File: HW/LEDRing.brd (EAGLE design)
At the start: 52.5 x 52.4 mm, 36 parts, among them U1 ATMEGA328P-AU, U2 MCP73831, U3 MIC5219 3.3V, U4 MMA8452Q, Y1 16MHZ

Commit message: Removed some files.
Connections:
- removed net VCCIO: U$1.4
- new net N$31: U$1.17, U$1.4
- net RESET: now also U$1.2
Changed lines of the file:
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@@
 <layer number="24" name="bOrigins" color="15" fill="1" visible="yes" active="yes"/>
 <layer number="25" name="tNames" color="7" fill="1" visible="yes" active="yes"/>
-<layer number="26" name="bNames" color="7" fill="1" visible="yes" active="yes"/>
+<layer number="26" name="bNames" color="7" fill="1" visible="no" active="yes"/>
 <layer number="27" name="tValues" color="7" fill="1" visible="yes" active="yes"/>
-<layer number="28" name="bValues" color="7" fill="1" visible="yes" active="yes"/>
+<layer number="28" name="bValues" color="7" fill="1" visible="no" active="yes"/>
 <layer number="29" name="tStop" color="7" fill="3" visible="no" active="yes"/>
 <layer number="30" name="bStop" color="7" fill="6" visible="no" active="yes"/>
@@
 <wire x1="23.241" y1="44.323" x2="21.717" y2="42.799" width="0.3048" layer="1"/>
 <wire x1="21.717" y1="42.799" x2="21.717" y2="30.988" width="0.3048" layer="1"/>
+<contactref element="U$1" pad="2"/>
+<wire x1="19.285" y1="23.341" x2="17.399" y2="30.988" width="0" layer="19" extent="1-16"/>
 </signal>
 <signal name="N$9">
@@
 <wire x1="16.51" y1="38.735" x2="16.51" y2="34.671" width="0.3048" layer="1"/>
 </signal>
-<signal name="VCCIO">
+<signal name="N$6">
+</signal>
+<signal name="N$31">
 <contactref element="U$1" pad="4"/>
-</signal>
-<signal name="N$6">
+<contactref element="U$1" pad="17"/>
+<wire x1="25.785" y1="16.029" x2="20.585" y2="23.341" width="0" layer="19" extent="16-16"/>
 </signal>
 </signals>

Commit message: Adding PCB changes for next version.
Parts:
- added C8: (no value), SparkFun-Capacitors:0603-CAP
- added D13: (no value), SparkFun-LED:LED-0603
- added JP1, JP2: JUMPER-3SMD, SparkFun-Retired:SJ_3
- added JP3: JUMPER-3-OLDSMD, SparkFun-Retired:SJ_3
- added LOGO1: OSHW-LOGOMINI, SparkFun-Aesthetics:OSHW-LOGO-MINI
- added R9: (no value), SparkFun-Passives:0603-RES
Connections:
- new net N$32: C8.1, U$1.2
- new net N$33: R9.2, U1.13
- new net N$34: D13.A, R9.1
- net GND: now also D13.C
- net RESET: now also C8.2; no longer U$1.2
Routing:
- net N$33: track 0.00 -> 22.9 mm, vias 0 -> 1
- net N$31: track 0.00 -> 11.1 mm, vias 0 -> 2
- net GND: track 202.6 -> 208.3 mm, vias 11 -> 12
- net N$32: track 0.00 -> 5.69 mm
- net 5V: track 63.7 -> 68.4 mm
- net N$4: track 14.1 -> 10.6 mm
- net RESET: track 33.6 -> 36.8 mm
- net N$15: track 33.3 -> 35.5 mm
- net V3_3: track 86.5 -> 88.4 mm
- net RX: track 10.9 -> 12.6 mm
- net N$34: track 0.00 -> 1.70 mm
- net VBATT: track 203.1 -> 204.8 mm
- net LED_DATA: track 59.5 -> 58.9 mm
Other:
- outline, holes or cut-outs redrawn

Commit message: Updated to version 1.1.
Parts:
- removed JP3: JUMPER-3-OLDSMD, SparkFun-Retired:SJ_3
- removed U$1: FT232R, GeekAmmo:SSOP-28
- added JP4: JUMPER-3SMD, SparkFun-Retired:SJ_3
- added R10: 0, SparkFun-Passives:0603-RES
- added U5: FT231XS, SparkFun-DigitalIC:SSOP20_L
- moved LOGO1 9.21 mm to (26.3, 13.8)
- moved C2 7.53 mm to (26.9, 16.8), turned to 225 degrees
- moved C4 7.49 mm to (23.4, 17.1), turned to 45 degrees
- moved J3 0.91 mm to (8.75, 24.7)
- moved D7 0.26 mm to (37.0, 44.6)
- moved D11 0.26 mm to (37.0, 7.21)
- moved D5 0.26 mm to (15.4, 44.6)
- moved D1 0.26 mm to (15.4, 7.21)
- moved D2 0.26 mm to (7.47, 15.1)
- moved D4 0.26 mm to (7.47, 36.7)
- moved D8 0.26 mm to (44.9, 36.7)
- moved D6 0.25 mm to (26.2, 47.5)
- moved D3 0.25 mm to (4.57, 25.9)
- moved D12 0.25 mm to (26.2, 4.32)
- moved D9 0.25 mm to (47.8, 25.9)
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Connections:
- removed net N$31: U$1.17, U$1.4
- removed net N$32: C8.1, U$1.2
- new net DTR: JP4.3, U5.1
- new net D_N_IN: JP1.1, JP2.1, U5.12
- new net D_N_OUT: JP1.2, U$2.P$2
- new net D_P_IN: JP1.3, JP2.3, U5.11
- new net D_P_OUT: JP2.2, U$2.P$3
- new net RTS: JP4.1, U5.2
- new net RTS_OR_DTR: C8.1, JP4.2
- net 5V: now also R10.2, U5.15; no longer U$1.20, U$2.P$1
- net GND: now also U5.16, U5.6; no longer U$1.18, U$1.21, U$1.25, U$1.26, U$1.7
- net N$4: now also R10.1, U$2.P$1; no longer U$1.16, U$2.P$2
- net N$5: now also U5.13, U5.14, U5.3; no longer U$1.15, U$2.P$3
- net RX: now also U5.20; no longer U$1.1
- net TX: now also U5.4; no longer U$1.5
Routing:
- net RTS_OR_DTR: track 0.00 -> 34.4 mm, vias 0 -> 2
- net D_P_IN: track 0.00 -> 25.7 mm, vias 0 -> 4
- net TX: track 9.58 -> 31.5 mm, vias 1 -> 4
- net D_N_IN: track 0.00 -> 18.0 mm
- net N$31: track 11.1 -> 0.00 mm, vias 2 -> 0
- net GND: track 208.3 -> 198.2 mm, vias 12 -> 13
- net RX: track 12.6 -> 21.8 mm, vias 2 -> 1
- net 5V: track 68.4 -> 61.3 mm
- net N$5: track 12.8 -> 7.05 mm
- net N$32: track 5.69 -> 0.00 mm
- net DTR: track 0.00 -> 4.54 mm
- net RTS: track 0.00 -> 4.50 mm
- net D_P_OUT: track 0.00 -> 2.77 mm
- net D_N_OUT: track 0.00 -> 2.32 mm
- net LED_DATA: track 58.9 -> 57.2 mm
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- added copper zone on layer 1, net N$31
- added copper zone on layer 16, net N$31
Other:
- outline, holes or cut-outs redrawn
- board text added: "(+)"
- board text added: "(-)"
- board text added: "DTR"
- board text added: "Diego Aguilera 15 Jan 2017"
- board text added: "M"
- board text added: "P"
- board text added: "RTS"
- board text added: "USB_M"
- board text added: "USB_P"
- board text added: "v1.1"
- board text removed: "Diego Aguilera 17 Nov 2016"
- board text removed: "v1.0"

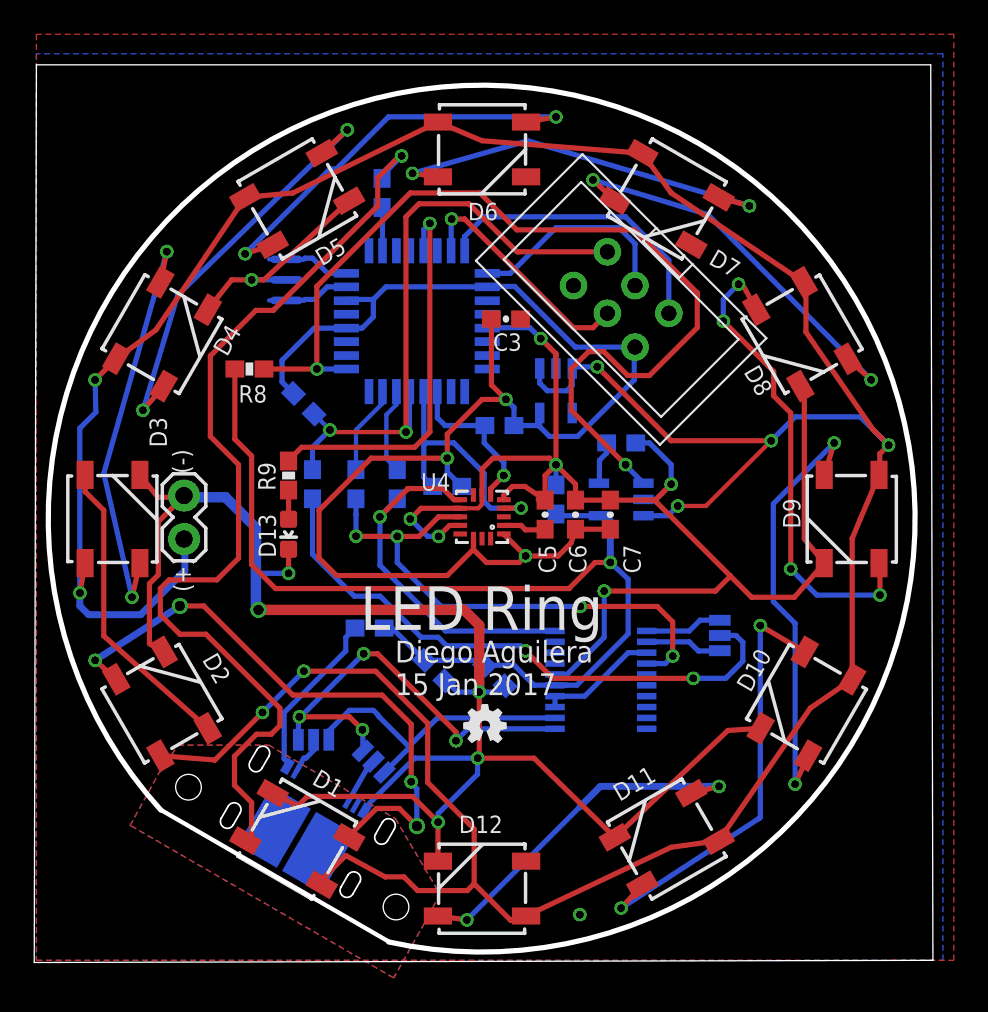
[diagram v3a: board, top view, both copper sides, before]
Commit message: Found error for USB part. Fixed. Still need to move usb to original spot.
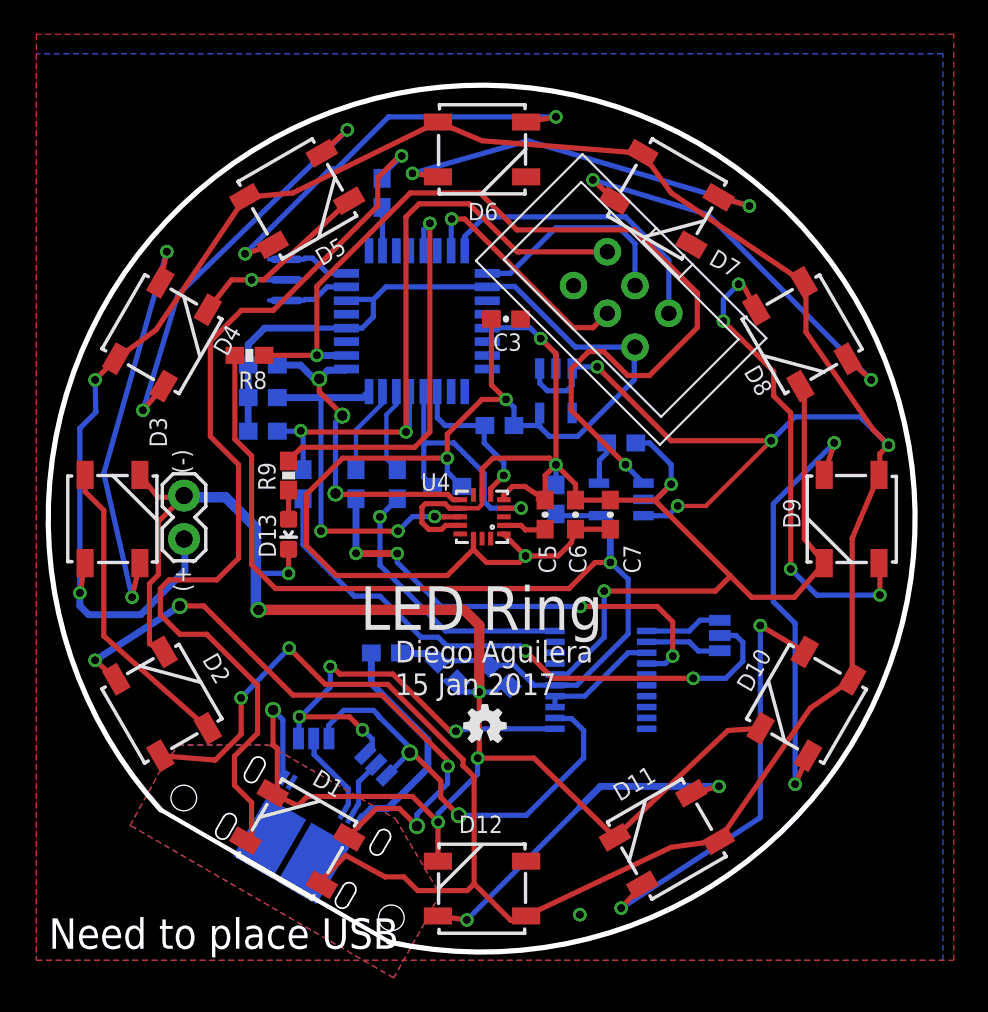
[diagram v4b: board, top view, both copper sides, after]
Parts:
- removed U$2: TE_USB_A121025CT, LEDRingLib:TE_USB_A121025CT
- added R11, R12: 10k, SparkFun-Passives:0603-RES
- added U$1: TE_USB_A121025CT, LEDRingLib:TE_USB_A121025CT
- moved JP1 3.93 mm to (20.0, 11.6), turned to 45 degrees
- moved JP2 3.75 mm to (16.3, 13.1), turned to 0 degrees
- moved R3 2.88 mm to (13.3, 31.0), turned to 0 degrees
- moved R10 1.73 mm to (20.5, 18.1)
- moved R8 0.80 mm to (12.6, 35.5)
- moved C4 0.75 mm to (24.1, 17.0)
- moved C8 0.55 mm to (15.7, 27.9)
- moved C2 0.25 mm to (27.2, 16.8)
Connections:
- new net INT1: R11.1, U1.32, U4.11
- new net INT2: R12.1, U1.1, U4.9
- net D_N_OUT: now also U$1.P$2; no longer U$2.P$2
- net D_P_OUT: now also U$1.P$3; no longer U$2.P$3
- net GND: now also U$1.P$5; no longer U$2.P$5
- net N$4: now also U$1.P$1; no longer U$2.P$1
- net RX: no longer U4.9
- net TX: no longer U4.11
- net V3_3: now also R11.2, R12.2
- net VSTAT: now also U1.2; no longer U1.1
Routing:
- net INT1: track 0.00 -> 21.8 mm, vias 0 -> 3
- net INT2: track 0.00 -> 19.5 mm, vias 0 -> 3
- net D_N_IN: track 18.0 -> 26.2 mm, vias 0 -> 2
- net V3_3: track 88.4 -> 94.5 mm
- net RX: track 21.8 -> 16.2 mm
- net TX: track 31.5 -> 27.4 mm
- net N$4: track 9.87 -> 13.4 mm
- net D_P_OUT: track 2.77 -> 5.21 mm
- net VBATT: track 203.7 -> 206.0 mm
- net N$15: track 35.3 -> 36.8 mm
- net RESET: track 36.8 -> 38.2 mm
- net D_N_OUT: track 2.32 -> 3.59 mm
- net GND: track 198.2 -> 199.4 mm, vias 13 -> 12
- net LED_DATA: track 57.2 -> 56.2 mm
- net VSTAT: track 56.5 -> 55.7 mm
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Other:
- board size 52.5 x 52.4 mm -> 50.6 x 50.6 mm
- board text added: "Need to place USB"

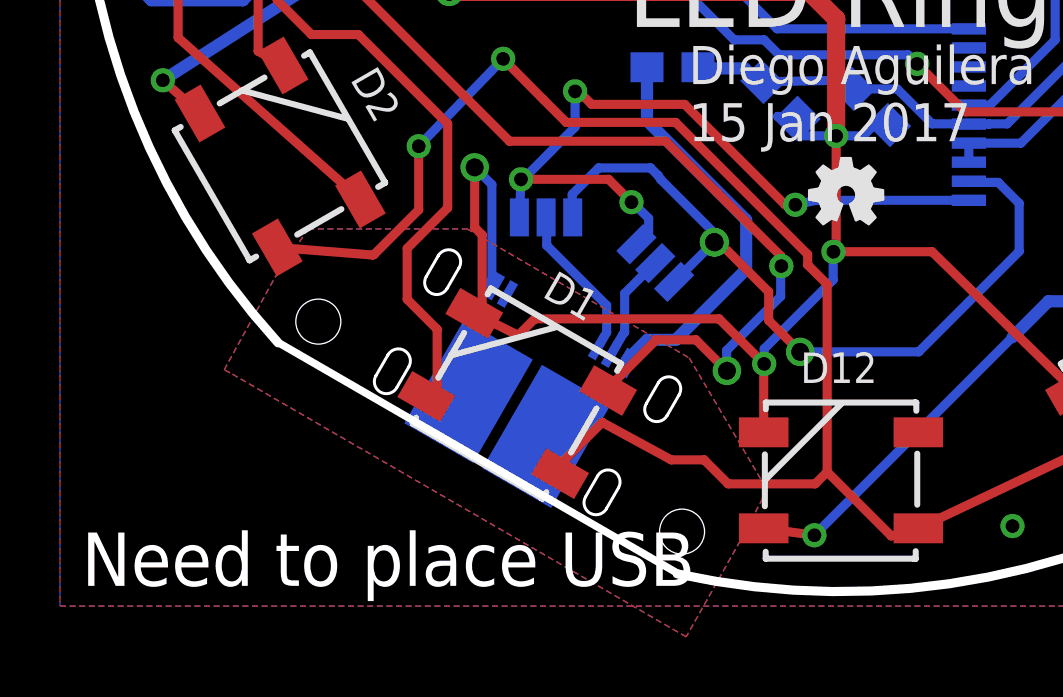
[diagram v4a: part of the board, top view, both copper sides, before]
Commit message: Moved USB connector.
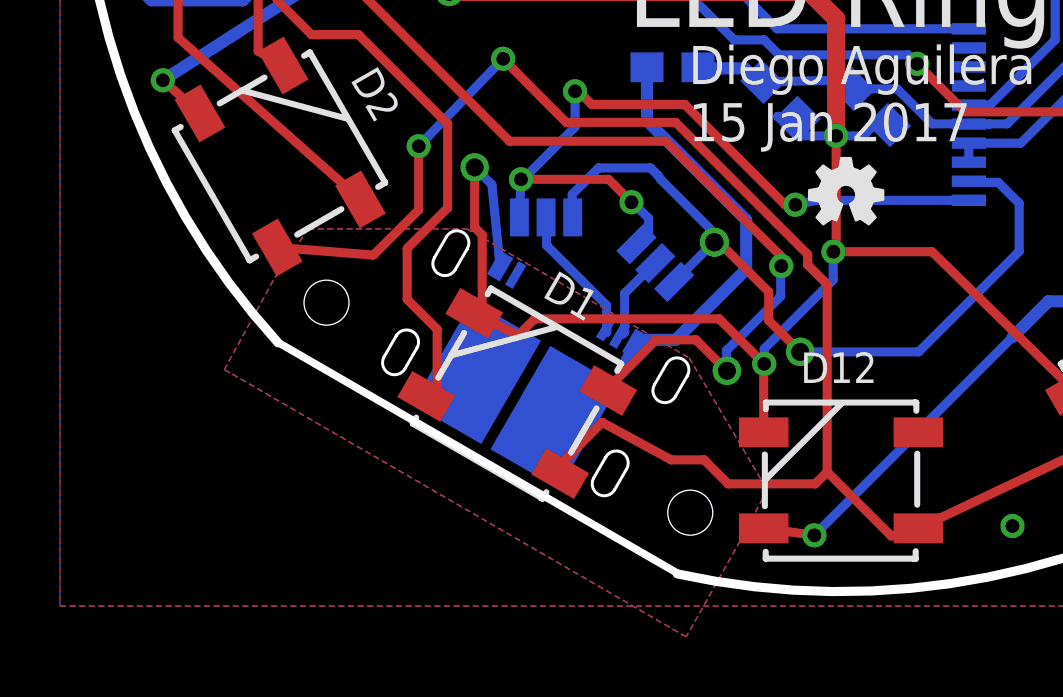
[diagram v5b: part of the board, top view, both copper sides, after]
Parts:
- moved U$1 0.69 mm to (14.2, 5.18)
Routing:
- net D_N_OUT: track 3.59 -> 2.93 mm
- net GND: track 199.4 -> 198.8 mm
- net N$4: track 13.4 -> 13.9 mm
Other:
- board text removed: "Need to place USB"
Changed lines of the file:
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@@
 <?xml version="1.0" encoding="utf-8"?>
 <!DOCTYPE eagle SYSTEM "eagle.dtd">
-<eagle version="7.7.0">
+<eagle version="7.3.0">
 <drawing>
 <settings>
@@
 <setting verticaltext="up"/>
 </settings>
-<grid distance="0.00196850394" unitdist="inch" unit="inch" style="lines" multiple="1" display="yes" altdistance="0.025" altunitdist="inch" altunit="inch"/>
+<grid distance="0.0500000001" unitdist="mm" unit="mm" style="lines" multiple="1" display="yes" altdistance="0.025" altunitdist="inch" altunit="mm"/>
 <layers>
 <layer number="1" name="Top" color="4" fill="1" visible="yes" active="yes"/>
@@
 <text x="9.1" y="28.7" size="1.016" layer="26" rot="R90">(-)</text>
 <text x="9.15" y="21.5" size="1.016" layer="26" rot="R90">(+)</text>
-<text x="0.85" y="0.8" size="1.778" layer="20">Need to place USB</text>
 </plain>
 <attributes>
@@
 <attribute name="VALUE" x="40.052" y="19.0039" size="0.02" layer="28" rot="MR90"/>
 </element>
-<element name="U$1" library="LEDRingLib" package="TE_USB_A121025CT" value="TE_USB_A121025CT" x="13.9" y="4.55" rot="MR210"/>
+<element name="U$1" library="LEDRingLib" package="TE_USB_A121025CT" value="TE_USB_A121025CT" x="14.1732" y="5.1816" rot="MR210"/>
 <element name="R11" library="SparkFun-Passives" package="0603-RES" value="10k" x="13.35" y="33" rot="MR0"/>
 <element name="R12" library="SparkFun-Passives" package="0603-RES" value="10k" x="13.35" y="34.9" rot="MR0"/>
@@
 <wire x1="13.95" y1="12.75" x2="13.95" y2="14.75" width="0.3048" layer="1"/>
 <via x="13.95" y="14.75" extent="1-16" drill="0.6" diameter="0.254" shape="octagon"/>
-<wire x1="14.523334375" y1="10.82964375" x2="14.523334375" y2="14.176665625" width="0.3048" layer="16"/>
+<wire x1="14.796534375" y1="11.46124375" x2="14.523334375" y2="14.176665625" width="0.3048" layer="16"/>
 <wire x1="14.523334375" y1="14.176665625" x2="13.95" y2="14.75" width="0.3048" layer="16"/>
 </signal>
@@
 <contactref element="JP1" pad="2"/>
 <contactref element="U$1" pad="P$2"/>
-<wire x1="18.507053125" y1="8.52964375" x2="18.9" y2="9.2" width="0.3048" layer="16"/>
+<wire x1="18.780253125" y1="9.16124375" x2="18.9" y2="9.2" width="0.3048" layer="16"/>
 <wire x1="18.9" y1="9.2" x2="18.95" y2="9.25" width="0.3048" layer="16"/>
 <wire x1="18.95" y1="9.25" x2="18.95" y2="10.55" width="0.3048" layer="16"/>
@@
 <wire x1="16.35" y1="12.15" x2="18.35" y2="10.15" width="0.3048" layer="16"/>
 <wire x1="18.35" y1="10.15" x2="18.35" y2="9.25" width="0.3048" layer="16"/>
-<wire x1="18.35" y1="9.25" x2="18.074040625" y2="8.77964375" width="0.3048" layer="16"/>
+<wire x1="18.35" y1="9.25" x2="18.347240625" y2="9.41124375" width="0.3048" layer="16"/>
 </signal>
 <signal name="D_N_IN">
@@
 <contactref element="R10" pad="1"/>
 <contactref element="U$1" pad="P$1"/>
-<wire x1="19.02666875" y1="8.22964375" x2="19.02666875" y2="8.32666875" width="0.4064" layer="16"/>
+<wire x1="19.29986875" y1="8.86124375" x2="19.02666875" y2="8.32666875" width="0.4064" layer="16"/>
 <wire x1="19.02666875" y1="8.32666875" x2="19.7" y2="9" width="0.4064" layer="16"/>
 <wire x1="19.7" y1="9" x2="20.65" y2="9" width="0.4064" layer="16"/>

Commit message: Added 0.1uF and 1000uF capacitors. (Need to finish) Added values for components.
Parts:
- added C10, C11, C12, C13, C14, C15, C16, C17, C18, C19, C20, C9: 0.1uF, SparkFun-Capacitors:0603-CAP
- added C21: 100uF, SparkFun-Capacitors:NIC_10X10.5_CAP
- C2, C3: value (none) -> 0.1uF
- R4, R8: value (none) -> 10k
- R7, R9: value (none) -> 200
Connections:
- net GND: now also C10.2, C11.2, C12.2, C13.2, C14.2, C15.2, C16.2, C17.2, C18.2, C19.2, C20.2, C9.2
- net VBATT: now also C10.1, C11.1, C12.1, C13.1, C14.1, C15.1, C16.1, C17.1, C18.1, C19.1, C20.1, C9.1
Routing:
- net VBATT: track 206.0 -> 209.6 mm, vias 8 -> 9

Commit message: Ready for next version? Should probably double check.
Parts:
- removed C10, C11, C12, C13, C14, C15, C16, C17, C18, C19, C20, C9: 0.1uF, SparkFun-Capacitors:0603-CAP
- removed C21: 100uF, SparkFun-Capacitors:NIC_10X10.5_CAP
- added R13: 10k, SparkFun-Passives:0603-RES
- added TP1: TEST-POINT3, SparkFun-Passives:PAD.03X.03
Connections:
- new net N$35: TP1.P$1, U$1.P$4
- net GND: no longer C10.2, C11.2, C12.2, C13.2, C14.2, C15.2, C16.2, C17.2, C18.2, C19.2, C20.2, C9.2
- net INT1: now also R13.1
- net RX: now also R13.2
- net VBATT: no longer C10.1, C11.1, C12.1, C13.1, C14.1, C15.1, C16.1, C17.1, C18.1, C19.1, C20.1, C9.1
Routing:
- net RX: track 16.2 -> 33.1 mm, vias 1 -> 2
- net INT1: track 21.8 -> 25.4 mm
- net VBATT: track 209.6 -> 206.4 mm, vias 9 -> 8
- net V3_3: track 94.5 -> 97.1 mm
- net 5V: track 60.5 -> 62.4 mm, vias 1 -> 2
- net N$35: track 0.00 -> 1.25 mm
- net GND: vias 12 -> 16
